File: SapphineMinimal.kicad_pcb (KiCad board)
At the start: 4 copper layers, 54.6 x 61 mm, 150 parts, among them IC201 DLHR-F50D-E1BD-C-NAV8, IC501 SLG59M1446V, J301 503182-1852, J401 Conn_01x01_Male, J402 Conn_01x04_Male, J403 ExtPPS, J501 JST, J801 USB_B_Micro, J802 Conn_02x05_Odd_Even, J803 Conn_02x05_Odd_Even, J805 Conn_01x04_Male, M701 AdafruitWINC1500, Q501 BC857BS, Q502 SSM3J378R,LXHF, SW801 EVQP7C01P, SW802 EVQP7C01P, U201 LIS2DH12TR, U202 BMP390, U301 MB85RS2MTAPNF-G-BDERE1, U402 SAM-M8Q-0-10, U501 TPS62150, U801 ATSAMD21G18A-A, U802 DS3231SN

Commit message: Midst of pretying layout
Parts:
- added R605: 47, Resistor_SMD:R_0603_1608Metric, B.Cu at (113.0, 120.6)
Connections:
- M701 pad 10: unconnected-(M701-Pad10) -> Net-(M701-Pad10)
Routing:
- net Net-(M701-Pad10): track 0.00 -> 4.14 mm
- net /Sapphire_Proc/SPARE: track 0.00 -> 1.91 mm, vias 0 -> 1
- net Net-(C401-Pad1): track 94.4 -> 95.8 mm
- net /SapphireMini_SD/SPI_SCK: track 89.6 -> 90.8 mm
- net /SapphireMini_GNSS/SAM_RESET: track 19.8 -> 18.6 mm
- net Net-(R304-Pad2): track 5.58 -> 6.54 mm
- net /I2C_SCL: track 122.1 -> 121.3 mm
- net /SapphireMini_GNSS/RS232_TXD: track 37.6 -> 36.8 mm
- net /SapphireMini_GNSS/SAM_TXD: track 27.0 -> 26.3 mm
- net /SapphireMini_SD/SPI_MISO: track 95.0 -> 95.6 mm
- net GND: track 157.8 -> 157.2 mm
- net /WIFI_IRQ: track 93.4 -> 94.0 mm
- net /SapphireMini_Power/VBUS: track 58.1 -> 58.5 mm, vias 2 -> 3
- net /P3V3: vias 19 -> 27
- added copper zone on F.Cu, net (none)
- added copper zone on In2.Cu, net /P3V3

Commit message: Prior to handsolder footprints
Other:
- board text added: "-SPI2-"
- board text added: "3V3"
- board text added: "CLK"
- board text added: "DIO"
- board text added: "MISO2"
- board text added: "MOSI2"
- board text added: "RST"
- board text added: "SCK2"
- board text added: "SPI2_CS"
- board text added: "SPI_CS"
- board text added: "WIFI_CS"
- board text added: "WiFi_CS"

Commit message: End of Day
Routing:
- net /P3V3: track 312.1 -> 334.0 mm, vias 27 -> 30
- net /SapphireMini_GNSS/RS232_RXD: track 41.6 -> 58.6 mm
- net /SapphireMini_SD/SPI_MOSI: track 82.3 -> 92.4 mm, vias 4 -> 6
- net /V_BKUP: track 45.3 -> 43.9 mm
- net /Sapphire_Proc/PB1: track 38.7 -> 39.9 mm
- net /Sapphire_Proc/RED_LED: track 46.6 -> 47.3 mm
- net /I2C_SDA: track 124.6 -> 124.0 mm
- net /DS3231/32KHz: track 41.0 -> 41.7 mm
- net /SapphireMini_SD/SPI_SCK: track 90.8 -> 91.4 mm, vias 4 -> 6
- net GND: track 157.2 -> 156.6 mm, vias 42 -> 65
- net /SapphireMini_SD/SPI_MISO: track 95.6 -> 95.5 mm, vias 5 -> 7
- added copper zone on F.Cu, net GND
- added copper zone on In1.Cu, net GND
- removed copper zone on F.Cu, net (none)
- removed copper zone on In2.Cu, net /P3V3
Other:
- board text added: "GNSS PPS"
- board text added: "GNSS PWR"

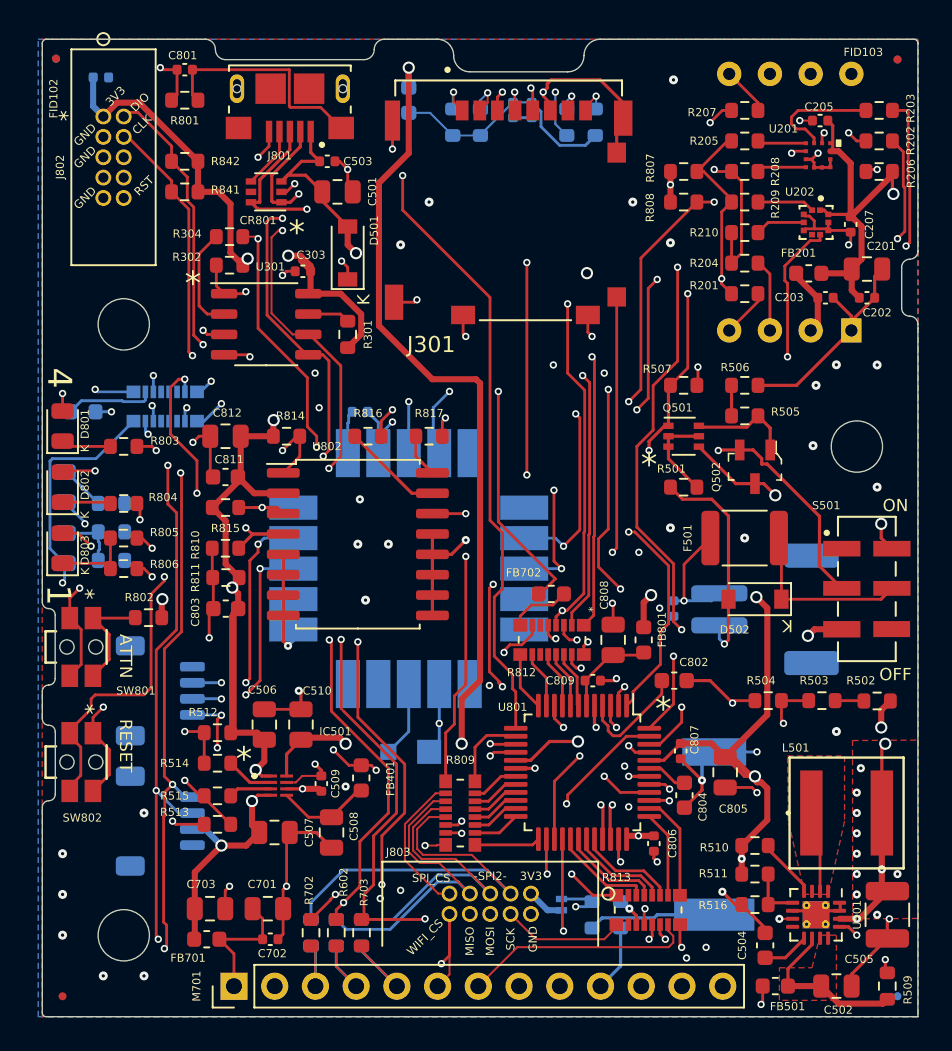
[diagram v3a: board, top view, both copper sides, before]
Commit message: Added hand solder pads
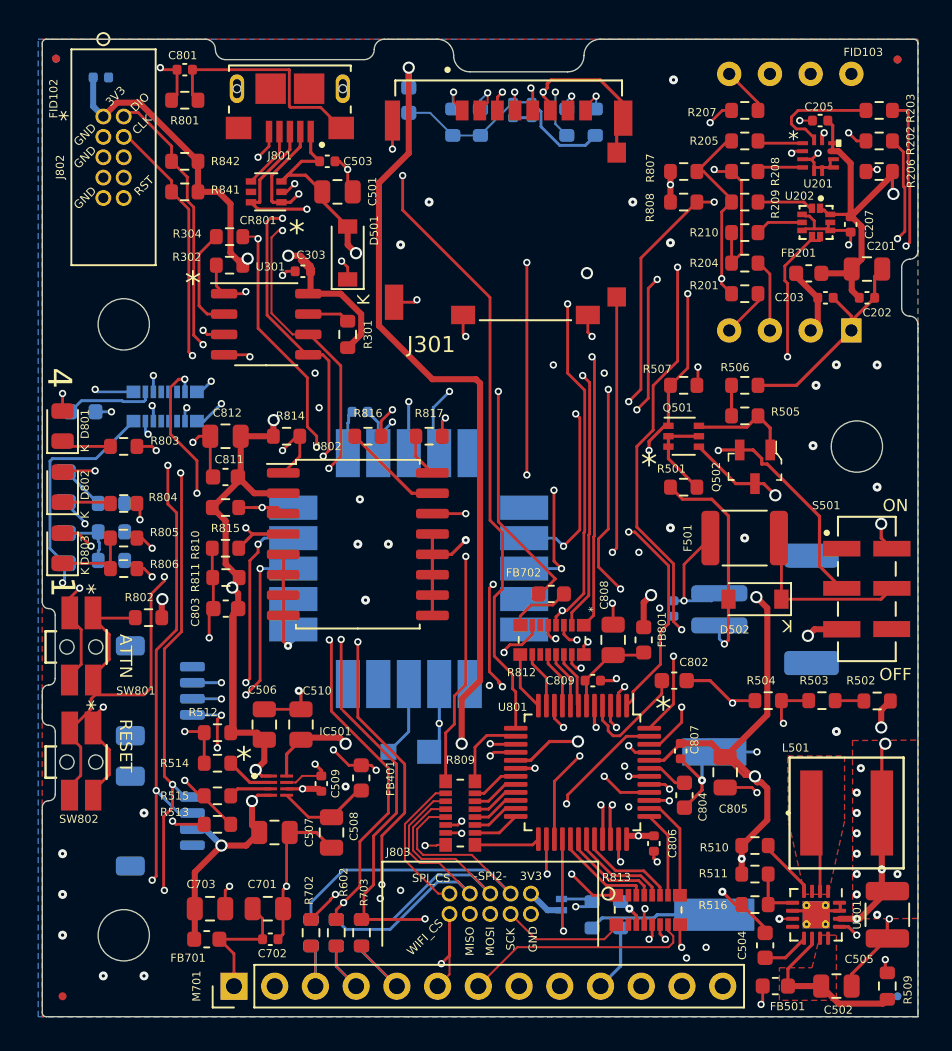
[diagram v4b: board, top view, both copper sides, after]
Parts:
- SW801: value EVQP7C01P -> EVQP7C/L_PAN; footprint Sapphire:EVQP7C01P -> Sapphire:EVQP7C01P_HandSolder
- SW802: value EVQP7C01P -> EVQP7C/L_PAN; footprint SapphineMinimal:EVQP7C01P -> Sapphire:EVQP7C01P_HandSolder
- U201: value LIS2DH12TR -> LGA-12_STM; footprint Sapphire:LIS2DH12TR -> Sapphire:LIS2DH12TR_Handsolder
- U202: footprint Sapphire:BMP388 -> Sapphire:BMP388_Handsolder
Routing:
- net /I2C_SCL: track 121.3 -> 119.0 mm
- net /I2C_SDA: track 124.0 -> 122.2 mm
- net /P3V3: track 334.0 -> 334.5 mm
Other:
- board text added: "For production remove hand solder pads for BMP388, LIS2DHH, SW push buttons, SW Slides"
- board text added: "Notes to FAB DS3231 contains a fragil 32KHz tuning fork. Avoid shocks when placing and depaneling boards DS3231 max reflow 2 times UBLOX receiver max reflow 1 time"
